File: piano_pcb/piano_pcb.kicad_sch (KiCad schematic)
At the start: 12 parts, among them J1 DIN-6, J2 DIN-6, Q1 FDN340P, U1 TB6612FNG

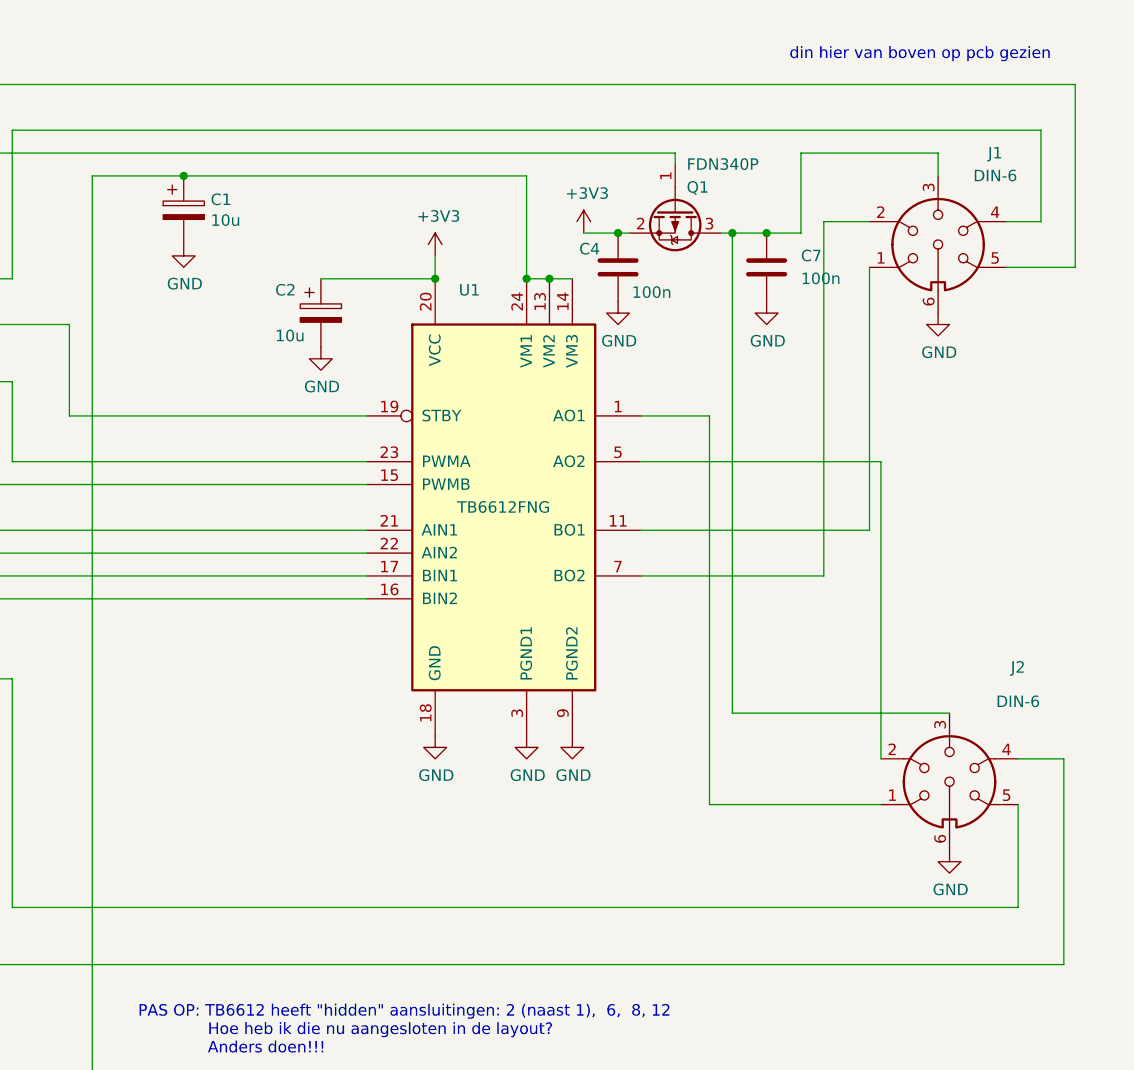
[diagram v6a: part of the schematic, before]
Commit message: Updated and added 3d picture
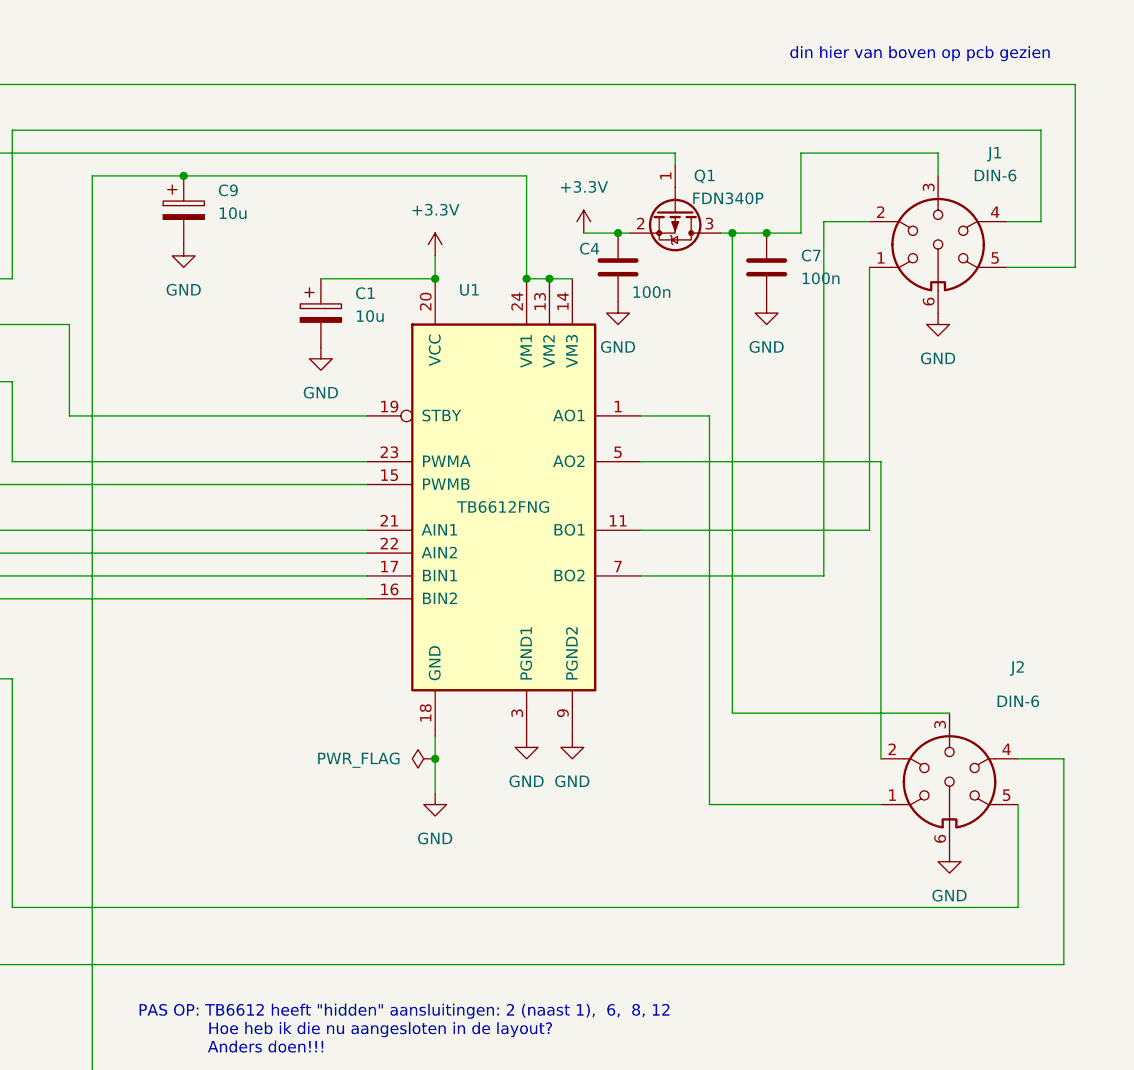
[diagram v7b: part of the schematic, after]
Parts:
- removed C1: 10u, Capacitor_Tantalum_SMD:CP_EIA-7343-30_AVX-N_HandSolder, symbol Device:CP
- removed C2: 10u, Capacitor_SMD:C_1210_3225Metric_Pad1.33x2.70mm_HandSolder, symbol Device:CP
- added C1, C9: 10u, Capacitor_Tantalum_SMD:CP_EIA-7343-30_AVX-N_HandSolder, symbol Device:C_Polarized
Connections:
- net Controller/Bat: now also C9.1
- net GND: now also C1.2, C9.2
- net +3V3 renamed +3.3V
- net +3.3V: now also C1.1
